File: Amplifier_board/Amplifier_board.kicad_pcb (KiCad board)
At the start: 2 copper layers, 100 x 100 mm, 175 parts, among them J1 Screw Terminal, J10 Conn_01x03_Pin, J11 Conn_01x03_Pin, J12 Conn_01x03_Pin, J13 Conn_01x03_Pin, J14 Conn_01x03_Pin, J15 Conn_01x03_Pin, J2 Screw Terminal, J3 Screw Terminal, J4 Screw Terminal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

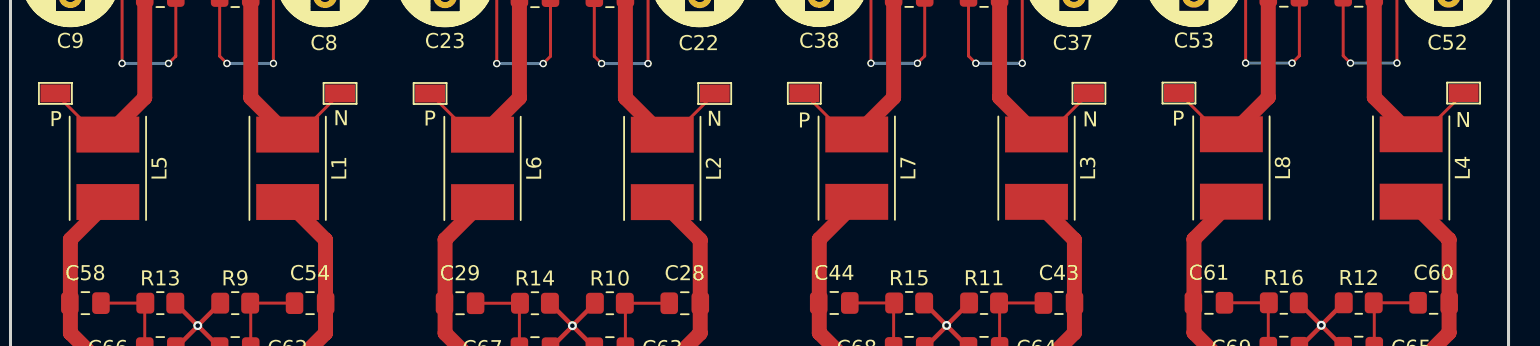
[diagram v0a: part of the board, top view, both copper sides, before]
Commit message: Added ferrites to amp board
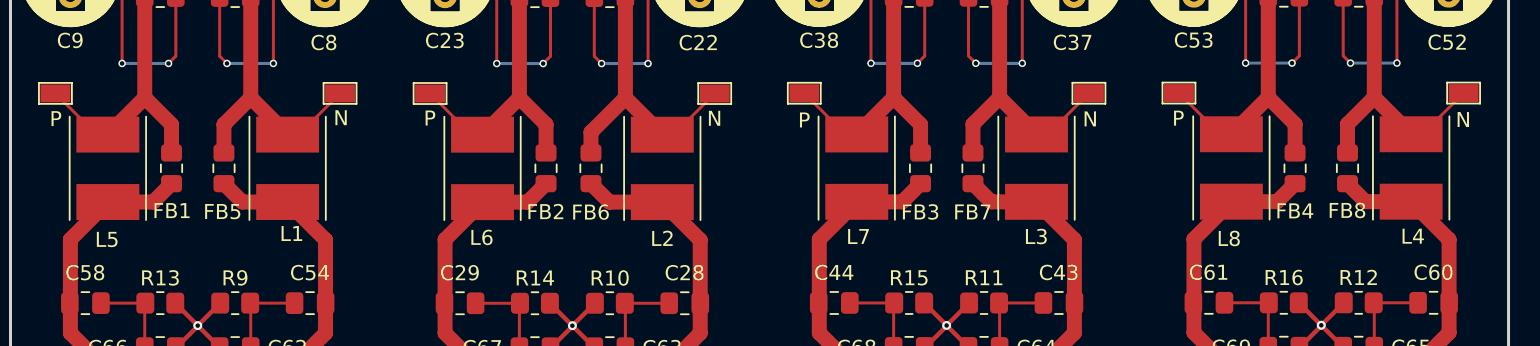
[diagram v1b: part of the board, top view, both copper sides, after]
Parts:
- added FB1: ILHB0805ER251V, Inductor_SMD:L_0805_2012Metric_Pad1.15x1.40mm_HandSolder, F.Cu at (85.2, 113.5)
- added FB2: ILHB0805ER251V, Inductor_SMD:L_0805_2012Metric_Pad1.15x1.40mm_HandSolder, F.Cu at (110.2, 113.5)
- added FB3: ILHB0805ER251V, Inductor_SMD:L_0805_2012Metric_Pad1.15x1.40mm_HandSolder, F.Cu at (135.2, 113.5)
- added FB4: ILHB0805ER251V, Inductor_SMD:L_0805_2012Metric_Pad1.15x1.40mm_HandSolder, F.Cu at (160.2, 113.5)
- added FB5: ILHB0805ER251V, Inductor_SMD:L_0805_2012Metric_Pad1.15x1.40mm_HandSolder, F.Cu at (88.8, 113.5)
- added FB6: ILHB0805ER251V, Inductor_SMD:L_0805_2012Metric_Pad1.15x1.40mm_HandSolder, F.Cu at (113.2, 113.5)
- added FB7: ILHB0805ER251V, Inductor_SMD:L_0805_2012Metric_Pad1.15x1.40mm_HandSolder, F.Cu at (138.8, 113.5)
- added FB8: ILHB0805ER251V, Inductor_SMD:L_0805_2012Metric_Pad1.15x1.40mm_HandSolder, F.Cu at (163.8, 113.5)
- C28, C29, C43, C44, C54, C58, C60, C61: value 2.2u -> 1000p
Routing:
- net /amp2/OutN: track 32.6 -> 37.9 mm
- net /amp3/OutP: track 32.6 -> 37.4 mm
- net /amp1/OutP: track 32.6 -> 37.4 mm
- net /amp1/OutN: track 32.4 -> 37.2 mm
- net /amp2/OutP: track 32.6 -> 37.3 mm
- net /amp4/OutN: track 34.7 -> 39.4 mm
- net /amp4/OutP: track 32.7 -> 37.4 mm
- net /amp3/OutN: track 32.6 -> 37.3 mm
- net /amp2/OutN_unfiltered: track 22.5 -> 27.1 mm
- net /amp4/OutP_unfiltered: track 22.3 -> 26.8 mm
- net /amp4/OutN_unfiltered: track 22.5 -> 26.9 mm
- net /amp3/OutP_unfiltered: track 22.3 -> 26.8 mm
- net /amp3/OutN_unfiltered: track 22.5 -> 26.9 mm
- net /amp1/OutP_unfiltered: track 22.3 -> 26.8 mm
- net /amp1/OutN_unfiltered: track 22.5 -> 26.9 mm
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
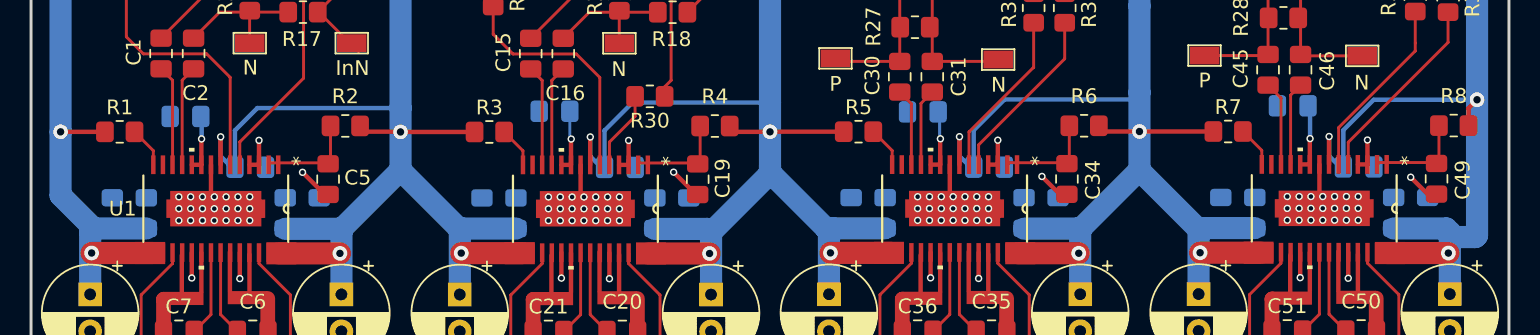
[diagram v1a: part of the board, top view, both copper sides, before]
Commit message: Separated AVDD and PVDD on amplifier board
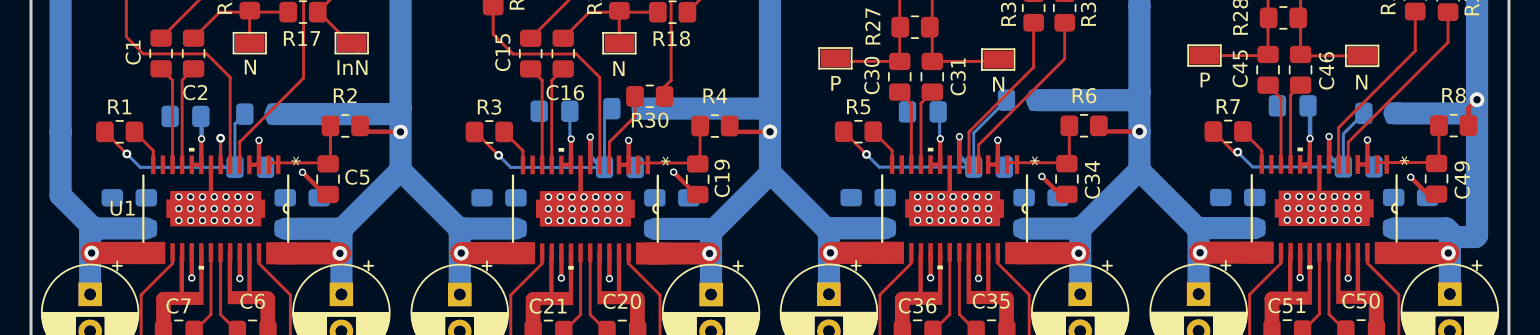
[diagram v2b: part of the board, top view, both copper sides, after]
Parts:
- added R37: 10, Capacitor_SMD:C_0805_2012Metric_Pad1.18x1.45mm_HandSolder, B.Cu at (90.0, 87.3)
- added R38: 10, Capacitor_SMD:C_0805_2012Metric_Pad1.18x1.45mm_HandSolder, B.Cu at (114.8, 86.9)
- added R39: 10, Capacitor_SMD:C_0805_2012Metric_Pad1.18x1.45mm_HandSolder, B.Cu at (141.5, 86.4)
- added R40: 10, Capacitor_SMD:C_0805_2012Metric_Pad1.18x1.45mm_HandSolder, B.Cu at (165.7, 87.2)
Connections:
- C17 pad 1: +24V -> /amp2/AVCC
- C3 pad 1: +24V -> /amp1/AVCC
- C32 pad 1: +24V -> /amp3/AVCC
- C47 pad 1: +24V -> /amp4/AVCC
- R1 pad 1: +24V -> /amp1/AVCC
- R3 pad 1: +24V -> /amp2/AVCC
- R5 pad 1: +24V -> /amp3/AVCC
- R7 pad 1: +24V -> /amp4/AVCC
- U1 pad 7: +24V -> /amp1/AVCC
- U2 pad 7: +24V -> /amp2/AVCC
- U3 pad 7: +24V -> /amp3/AVCC
- U4 pad 7: +24V -> /amp4/AVCC
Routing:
- net +24V: track 622.9 -> 559.2 mm, vias 20 -> 15
- net /amp3/AVCC: track 0.00 -> 20.1 mm, vias 0 -> 2
- net /amp4/AVCC: track 0.00 -> 18.8 mm, vias 0 -> 2
- net /amp2/AVCC: track 0.00 -> 18.3 mm, vias 0 -> 2
- net /amp1/AVCC: track 0.00 -> 18.1 mm, vias 0 -> 2

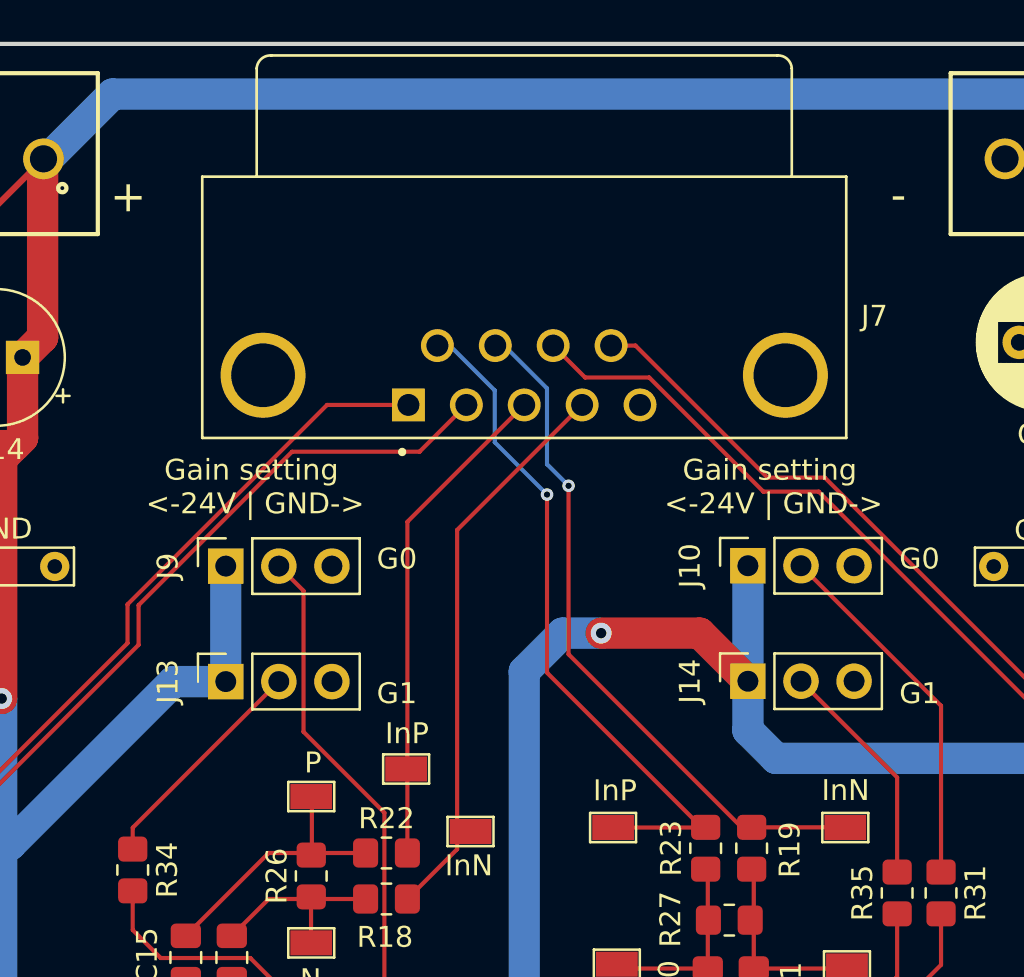
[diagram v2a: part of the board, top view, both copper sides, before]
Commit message: Updated ribbon connector on amp board
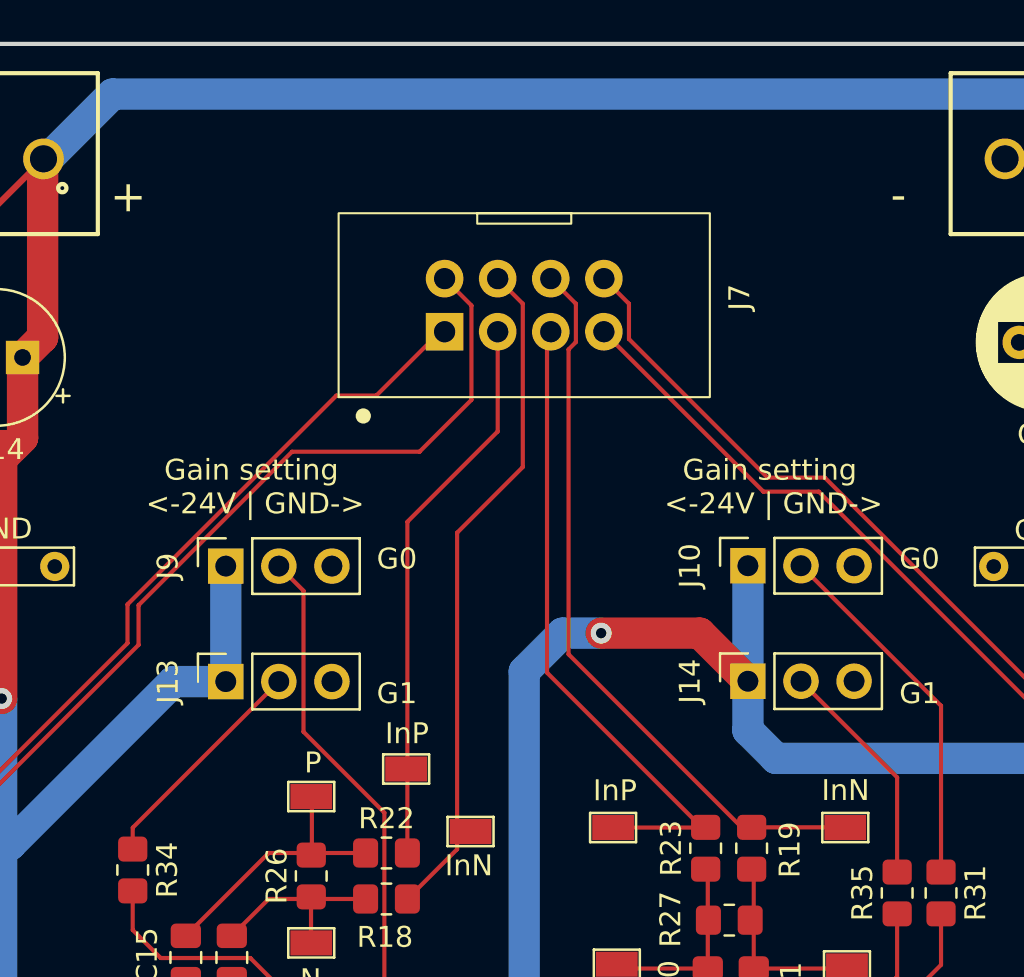
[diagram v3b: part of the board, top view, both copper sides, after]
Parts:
- J7: value A-DF_09_A_KG-T4S -> Conn_02x04_Odd_Even; footprint project_lib:ASSMANN_A-DF_09_A_KG-T4S -> project_lib:BHR-08-VUA
- moved J7 7.31 mm to (124.5, 52.0), turned to 90 degrees
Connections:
- J7 pad 5: unconnected-(J7-Pad5) -> /In3P
- J7 pad 6: /In3P -> /In3N
- J7 pad 7: /In3N -> /In4P
- J7 pad 8: /In4P -> /In4N
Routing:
- net /In1N: track 42.6 -> 49.3 mm
- net /In2N: track 27.2 -> 32.5 mm
- net /In1P: track 39.2 -> 43.0 mm
- net /In2P: track 23.9 -> 27.3 mm
- net /In4N: track 45.3 -> 48.0 mm
- net /In3N: track 33.2 -> 35.4 mm, vias 1 -> 0
- net /In4P: track 46.4 -> 44.3 mm
- net /In3P: track 33.8 -> 32.0 mm, vias 1 -> 0

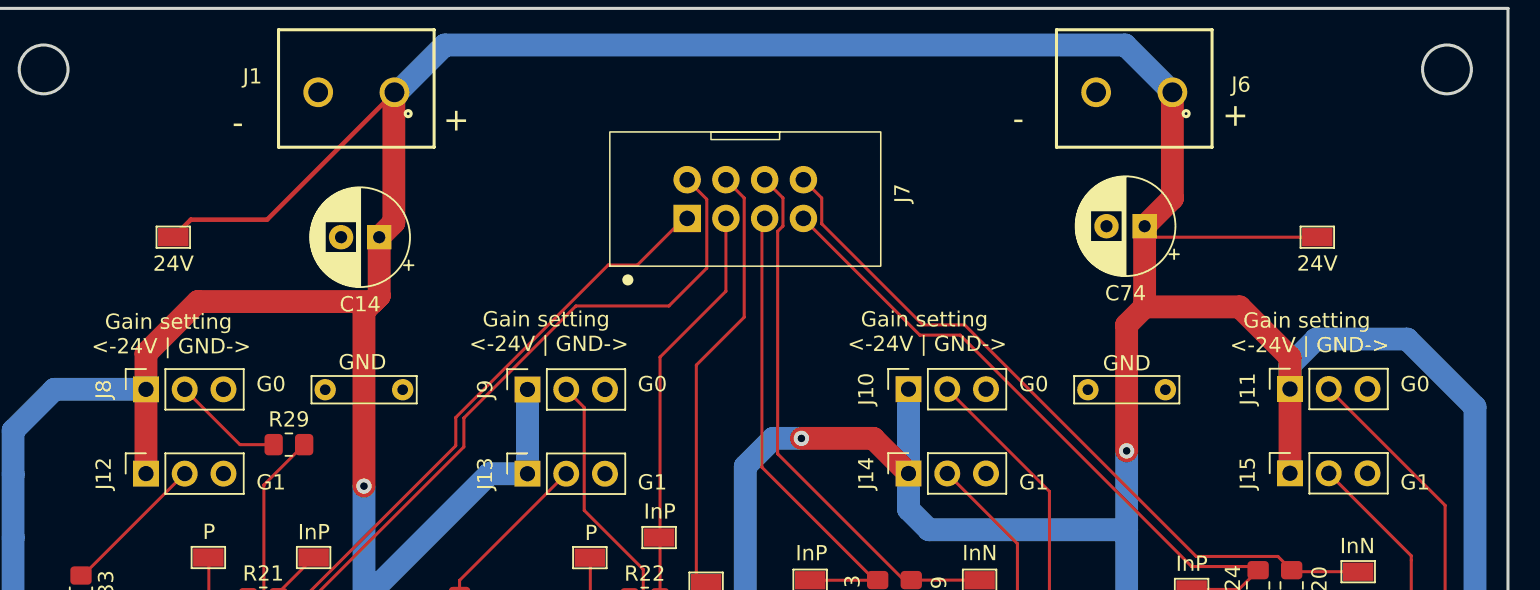
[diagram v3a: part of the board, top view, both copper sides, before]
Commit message: Changed to 4 layer board
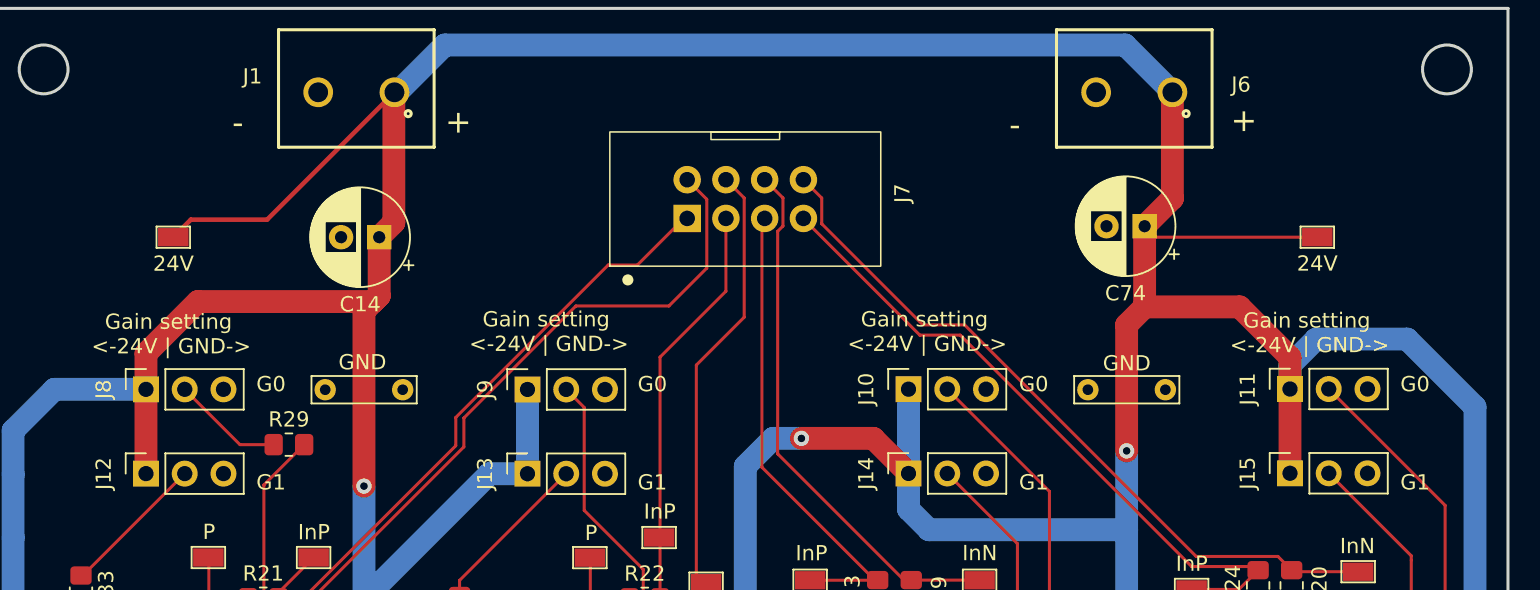
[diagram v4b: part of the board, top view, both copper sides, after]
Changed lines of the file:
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@@
 				(font
 					(size 1 1)
-					(thickness 0.1)
+					(thickness 0.15)
 				)
 			)
@@
 			(font
 				(size 1 1)
-				(thickness 0.1)
+				(thickness 0.15)
 			)
 			(justify left bottom)
@@
 	)
 	(gr_text "+"
-		(at 104.69 47.69 0)
+		(at 104.825 47.825 0)
 		(layer "F.SilkS")
 		(effects
 			(font
 				(size 1.5 1.5)
-				(thickness 0.1)
+				(thickness 0.15)
 			)
 			(justify left bottom)
@@
 			(font
 				(size 1 1)
-				(thickness 0.1)
+				(thickness 0.15)
 			)
 			(justify left bottom)
@@
 			(font
 				(size 1 1)
-				(thickness 0.1)
+				(thickness 0.15)
 			)
 			(justify left bottom)
@@
 			(font
 				(size 1 1)
-				(thickness 0.1)
+				(thickness 0.15)
 			)
 			(justify left bottom)
@@
 	)
 	(gr_text "+"
-		(at 155.77 47.38 0)
+		(at 156.325 47.725 0)
 		(layer "F.SilkS")
 		(effects
 			(font
 				(size 1.5 1.5)
-				(thickness 0.1)
+				(thickness 0.15)
 			)
 			(justify left bottom)
@@
 			(font
 				(size 1 1)
-				(thickness 0.1)
+				(thickness 0.15)
 			)
 			(justify left bottom)
@@
 			(font
 				(size 1.5 1.5)
-				(thickness 0.1)
+				(thickness 0.15)
 			)
 			(justify left bottom)
@@
 			(font
 				(size 1 1)
-				(thickness 0.1)
+				(thickness 0.15)
 			)
 			(justify left bottom)
@@
 			(font
 				(size 1 1)
-				(thickness 0.1)
+				(thickness 0.15)
 			)
 			(justify left bottom)
@@
 			(font
 				(size 1 1)
-				(thickness 0.1)
+				(thickness 0.15)
 			)
 			(justify left bottom)
@@
 	)
 	(gr_text "-"
-		(at 142.03 47.62 0)
+		(at 141.8 48.025 0)
 		(layer "F.SilkS")
 		(effects
 			(font
 				(size 1.5 1.5)
-				(thickness 0.1)
+				(thickness 0.15)
 			)
 			(justify left bottom)

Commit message: Amp board final draft
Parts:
- C10, C11, C12, C13, C24, C25, C26, C27, C39, C40, C41, C42, C55, C56, C57, C59: moved to F.Cu
- moved C13 5.53 mm to (97.1, 95.2)
- moved C40 3.63 mm to (147.4, 95.2)
- moved C55 3.16 mm to (152.1, 95.2)
- moved C39 3.11 mm to (127.1, 95.1)
- moved C42 3.07 mm to (144.5, 95.2)
- moved C25 3.07 mm to (121.9, 95.0)
- moved C24 3.05 mm to (102.2, 95.2)
- moved C41 2.65 mm to (129.9, 95.1)
- moved C57 2.62 mm to (155.0, 95.2)
- moved C26 2.51 mm to (105.1, 95.2)
- moved C27 2.51 mm to (119.0, 95.0)
- moved C49 2.32 mm to (168.7, 89.5)
- moved C10 2.30 mm to (77.7, 94.0)
- moved C12 2.28 mm to (80.2, 94.9)
- moved C56 2.23 mm to (171.0, 95.0)
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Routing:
- net +24V: track 559.2 -> 506.7 mm, vias 15 -> 23
- net GND: track 79.0 -> 123.3 mm, vias 104 -> 108
- net Net-(U4-*FAULT): track 7.07 -> 6.38 mm
- net Net-(U2-*FAULT): track 7.07 -> 7.60 mm
- added copper zone on F.Cu, net +24V
